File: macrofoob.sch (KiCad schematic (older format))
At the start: 90 parts, among them J2 LED_DATA, J3 POWER, J4 MATRIX_COLUMNS, J5 MATRIX_ROWS, J6 I2C, J7 SSD1306 128x32 OLED, Q1 2N 2222A, SW1 Switch, SW10 Switch, SW11 Switch, SW12 Switch, SW13 Switch, SW14 Switch, SW15 Switch, SW16 Switch, SW17 Switch, SW18 Switch, SW19 Switch, SW2 Switch, SW20 Switch, SW21 Switch, SW22 Switch, SW23 Switch, SW24 Switch, SW25 Switch, SW26 SW_Reset, SW3 Switch, SW4 Switch, SW5 Switch, SW6 Switch, SW7 Switch, SW8 Switch, SW9 Switch

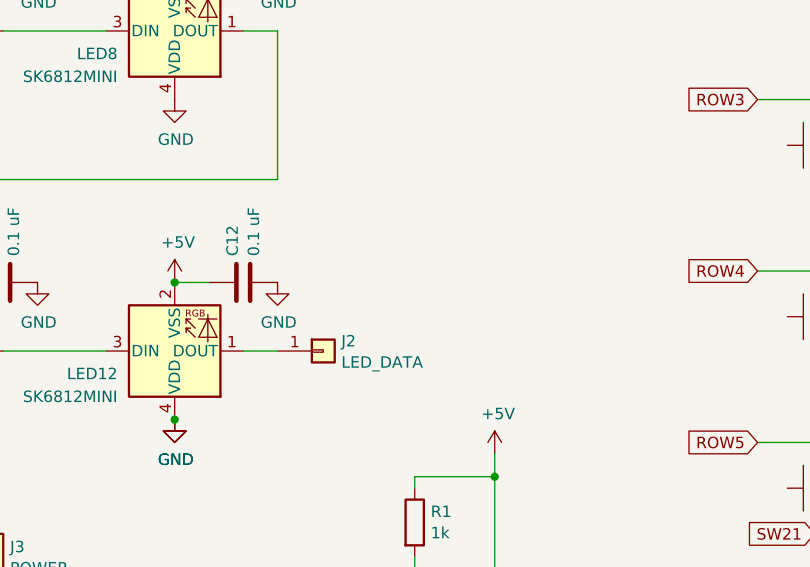
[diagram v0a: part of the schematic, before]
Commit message: updated schematic with more backlight options
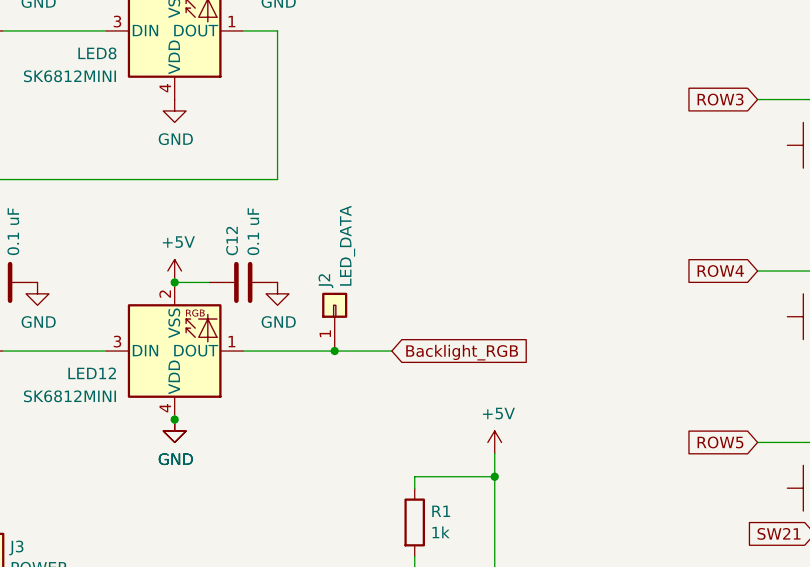
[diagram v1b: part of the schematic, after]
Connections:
- net Backlight_RGB: now reaches J2.1 (Pin_1), LED12.1 (DOUT)
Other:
- moved on the sheet: J2
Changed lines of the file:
@@
 L Connector_Generic:Conn_01x01 J2
 U 1 1 5D751619
-P 5350 4100
-F 0 "J2" H 5429 4143 50  0000 L CNN
-F 1 "LED_DATA" H 5429 4050 50  0000 L CNN
-F 2 "testatur:Generic_Pads_2mm_1x1" H 5350 4100 50  0001 C CNN
-F 3 "~" H 5350 4100 50  0001 C CNN
-	1    5350 4100
-	1    0    0    -1
+P 5400 3900
+F 0 "J2" H 5479 3943 50  0000 L CNN
+F 1 "LED_DATA" H 5479 3850 50  0000 L CNN
+F 2 "testatur:Generic_Pads_2mm_1x1" H 5400 3900 50  0001 C CNN
+F 3 "~" H 5400 3900 50  0001 C CNN
+	1    5400 3900
+	0    -1   -1   0
 $EndComp
-Wire Wire Line
-	5000 4100 5150 4100
 $Comp
 L Connector_Generic:Conn_01x05 J4
@@
 	0    1    1    0
 $EndComp
+Text GLabel 5650 4100 2    50   Input ~ 0
+Backlight_RGB
+Wire Wire Line
+	5000 4100 5400 4100
+Wire Wire Line
+	5400 4100 5650 4100
+Connection ~ 5400 4100
 $EndSCHEMATC

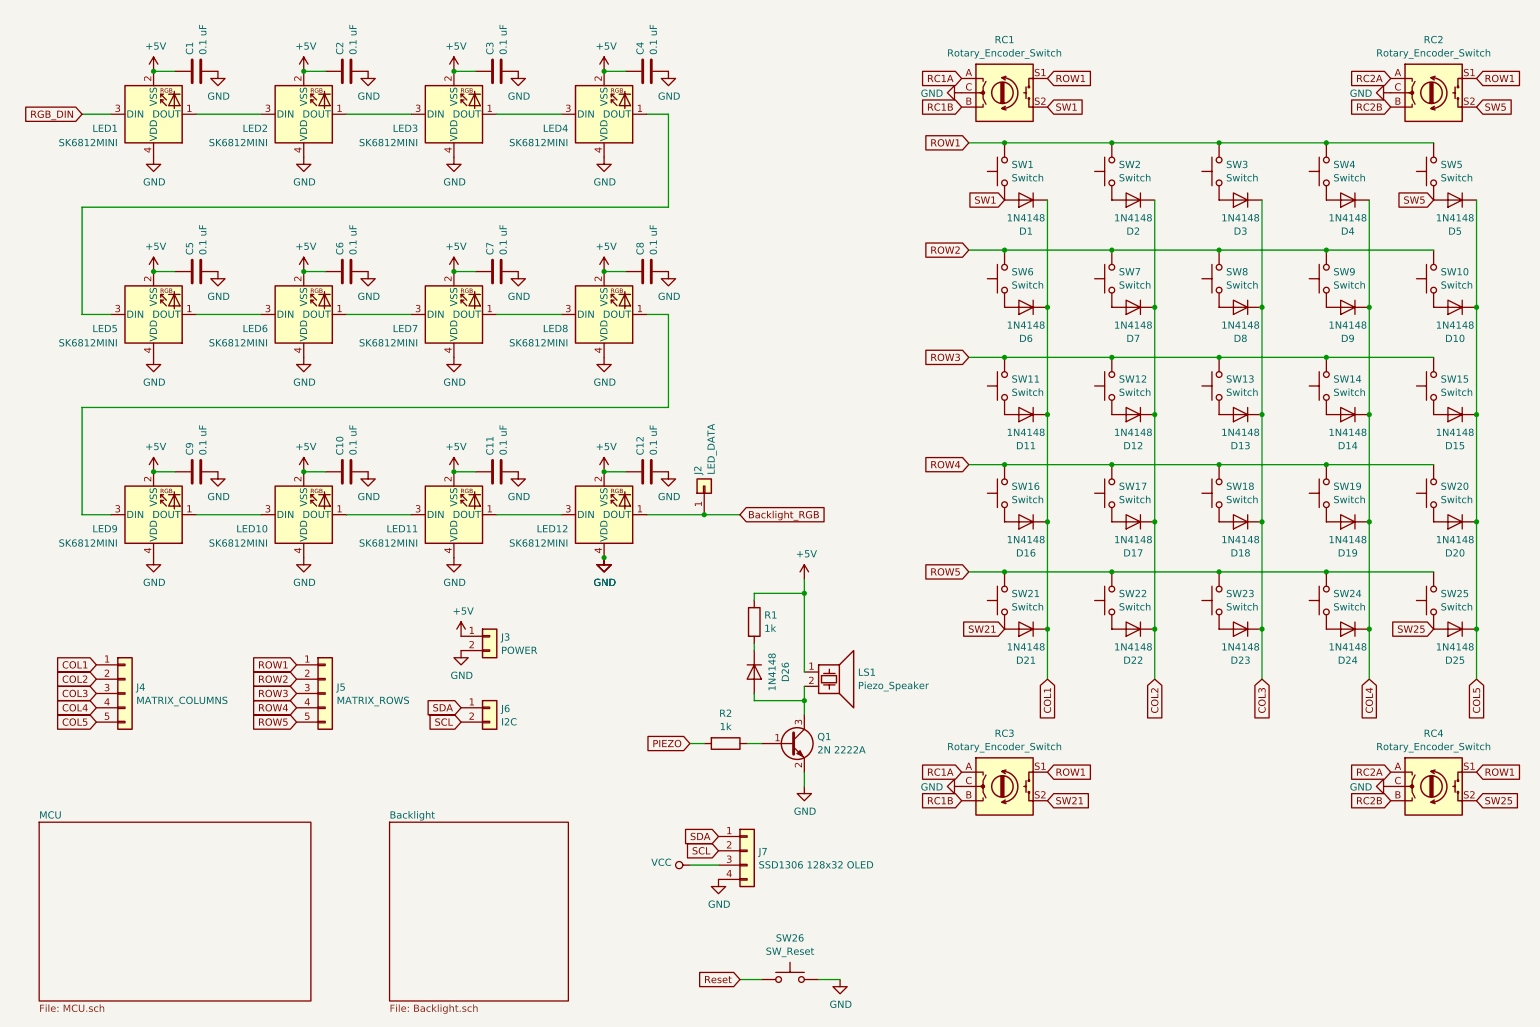
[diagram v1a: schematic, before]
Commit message: new component annotations
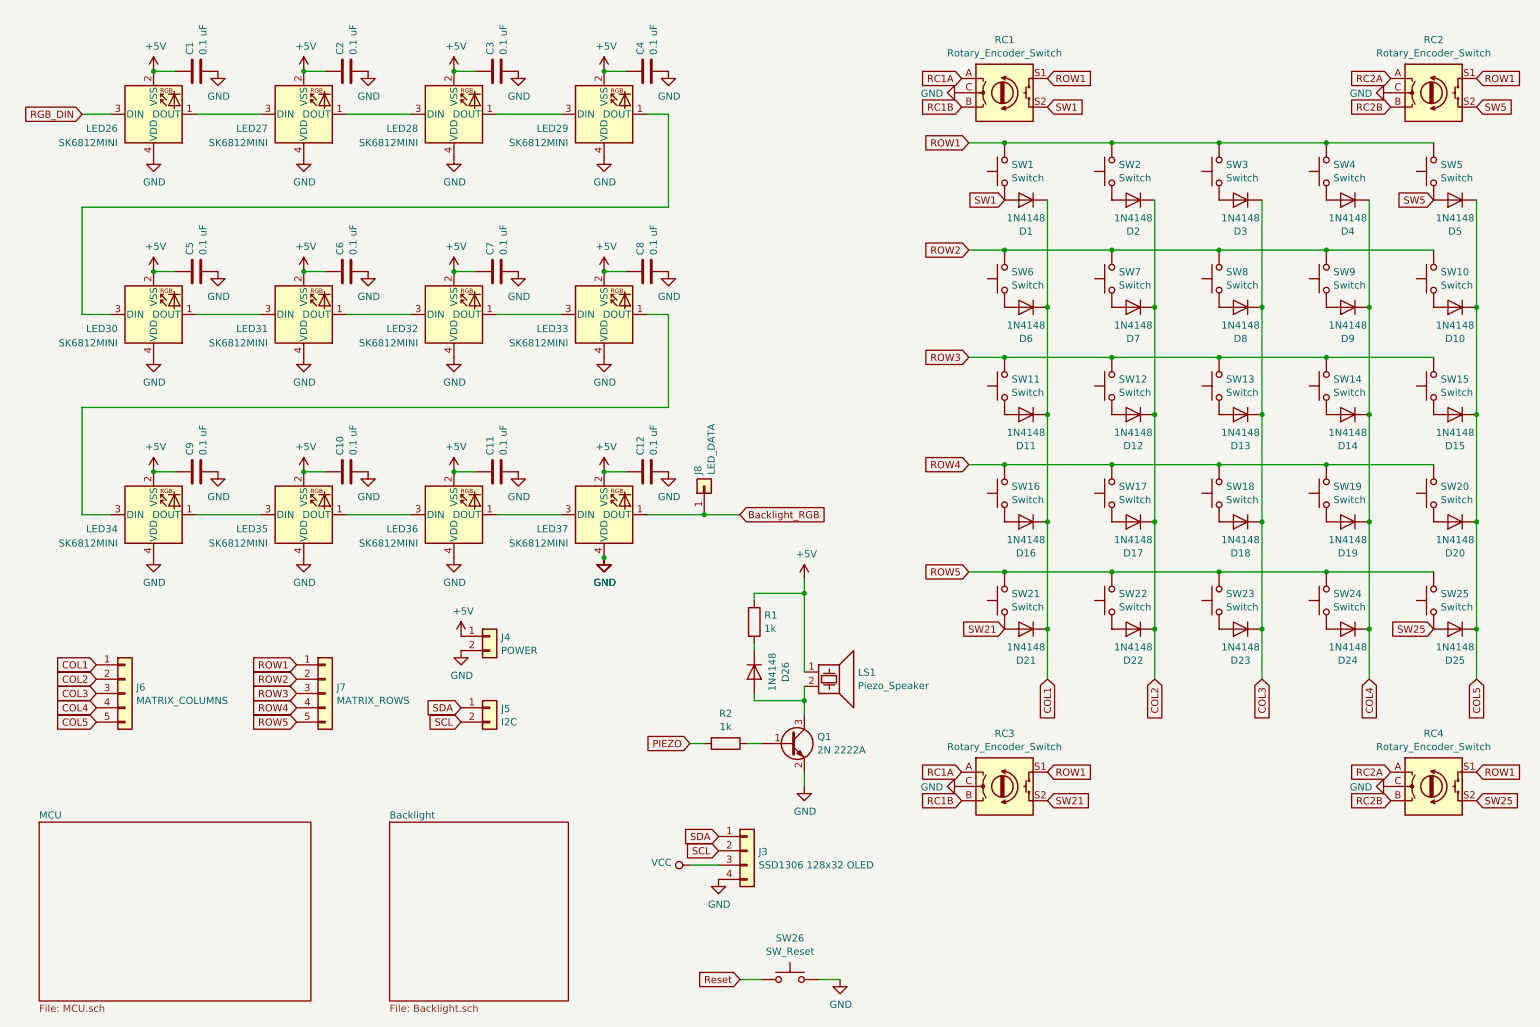
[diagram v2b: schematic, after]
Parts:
- renumbered J7 to J3, J3 to J4, J6 to J5, J4 to J6, J5 to J7, J2 to J8, LED1 to LED26, LED2 to LED27, LED3 to LED28, LED4 to LED29, LED5 to LED30, LED6 to LED31, LED7 to LED32, LED8 to LED33, LED9 to LED34, LED10 to LED35, LED11 to LED36, LED12 to LED37
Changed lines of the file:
@@
 Connection ~ 10800 4150
 $Comp
-L LED:SK6812MINI LED1
+L LED:SK6812MINI LED26
 U 1 1 5D82654C
 P 1550 1300
-F 0 "LED1" H 1300 1400 50  0000 R CNN
+F 0 "LED26" H 1300 1400 50  0000 R CNN
 F 1 "SK6812MINI" H 1300 1500 50  0000 R CNN
 F 2 "LED_SMD:LED_SK6812MINI_PLCC4_3.5x3.5mm_P1.75mm" H 1600 1000 50  0001 L TNN
@@
 $EndComp
 $Comp
-L power:GND #PWR041
+L power:GND #PWR044
 U 1 1 5D9F102E
 P 7200 6000
-F 0 "#PWR041" H 7200 5750 50  0001 C CNN
+F 0 "#PWR044" H 7200 5750 50  0001 C CNN
 F 1 "GND" V 7205 5871 50  0000 R CNN
 F 2 "" H 7200 6000 50  0001 C CNN
@@
 $EndComp
 $Comp
-L power:GND #PWR042
+L power:GND #PWR045
 U 1 1 5D9F103A
 P 10200 6000
-F 0 "#PWR042" H 10200 5750 50  0001 C CNN
+F 0 "#PWR045" H 10200 5750 50  0001 C CNN
 F 1 "GND" V 10205 5871 50  0000 R CNN
 F 2 "" H 10200 6000 50  0001 C CNN
@@
 SW25
 $Comp
-L LED:SK6812MINI LED2
+L LED:SK6812MINI LED27
 U 1 1 5DA35698
 P 2600 1300
-F 0 "LED2" H 2350 1400 50  0000 R CNN
+F 0 "LED27" H 2350 1400 50  0000 R CNN
 F 1 "SK6812MINI" H 2350 1500 50  0000 R CNN
 F 2 "LED_SMD:LED_SK6812MINI_PLCC4_3.5x3.5mm_P1.75mm" H 2650 1000 50  0001 L TNN
@@
 Connection ~ 2600 1000
 $Comp
-L LED:SK6812MINI LED3
+L LED:SK6812MINI LED28
 U 1 1 5DA392F5
 P 3650 1300
-F 0 "LED3" H 3400 1400 50  0000 R CNN
+F 0 "LED28" H 3400 1400 50  0000 R CNN
 F 1 "SK6812MINI" H 3400 1500 50  0000 R CNN
 F 2 "LED_SMD:LED_SK6812MINI_PLCC4_3.5x3.5mm_P1.75mm" H 3700 1000 50  0001 L TNN
@@
 Connection ~ 3650 1000
 $Comp
-L LED:SK6812MINI LED4
+L LED:SK6812MINI LED29
 U 1 1 5DA3CFEE
 P 4700 1300
-F 0 "LED4" H 4450 1400 50  0000 R CNN
+F 0 "LED29" H 4450 1400 50  0000 R CNN
 F 1 "SK6812MINI" H 4450 1500 50  0000 R CNN
 F 2 "LED_SMD:LED_SK6812MINI_PLCC4_3.5x3.5mm_P1.75mm" H 4750 1000 50  0001 L TNN
@@
 	3950 1300 4400 1300
 $Comp
-L LED:SK6812MINI LED5
+L LED:SK6812MINI LED30
 U 1 1 5DA540F9
 P 1550 2700
-F 0 "LED5" H 1300 2800 50  0000 R CNN
+F 0 "LED30" H 1300 2800 50  0000 R CNN
 F 1 "SK6812MINI" H 1300 2900 50  0000 R CNN
 F 2 "LED_SMD:LED_SK6812MINI_PLCC4_3.5x3.5mm_P1.75mm" H 1600 2400 50  0001 L TNN
@@
 Connection ~ 1550 2400
 $Comp
-L LED:SK6812MINI LED6
+L LED:SK6812MINI LED31
 U 1 1 5DA54119
 P 2600 2700
-F 0 "LED6" H 2350 2800 50  0000 R CNN
+F 0 "LED31" H 2350 2800 50  0000 R CNN
 F 1 "SK6812MINI" H 2350 2900 50  0000 R CNN
 F 2 "LED_SMD:LED_SK6812MINI_PLCC4_3.5x3.5mm_P1.75mm" H 2650 2400 50  0001 L TNN
@@
 Connection ~ 2600 2400
 $Comp
-L LED:SK6812MINI LED7
+L LED:SK6812MINI LED32
 U 1 1 5DA54139
 P 3650 2700
-F 0 "LED7" H 3400 2800 50  0000 R CNN
+F 0 "LED32" H 3400 2800 50  0000 R CNN
 F 1 "SK6812MINI" H 3400 2900 50  0000 R CNN
 F 2 "LED_SMD:LED_SK6812MINI_PLCC4_3.5x3.5mm_P1.75mm" H 3700 2400 50  0001 L TNN
@@
 Connection ~ 3650 2400
 $Comp
-L LED:SK6812MINI LED8
+L LED:SK6812MINI LED33
 U 1 1 5DA54159
 P 4700 2700
-F 0 "LED8" H 4450 2800 50  0000 R CNN
+F 0 "LED33" H 4450 2800 50  0000 R CNN
 F 1 "SK6812MINI" H 4450 2900 50  0000 R CNN
 F 2 "LED_SMD:LED_SK6812MINI_PLCC4_3.5x3.5mm_P1.75mm" H 4750 2400 50  0001 L TNN
@@
 	3950 2700 4400 2700
 $Comp
-L LED:SK6812MINI LED9
+L LED:SK6812MINI LED34
 U 1 1 5DA5C5A4
 P 1550 4100
-F 0 "LED9" H 1300 4200 50  0000 R CNN
+F 0 "LED34" H 1300 4200 50  0000 R CNN
 F 1 "SK6812MINI" H 1300 4300 50  0000 R CNN
 F 2 "LED_SMD:LED_SK6812MINI_PLCC4_3.5x3.5mm_P1.75mm" H 1600 3800 50  0001 L TNN
@@
 Connection ~ 1550 3800
 $Comp
-L LED:SK6812MINI LED10
+L LED:SK6812MINI LED35
 U 1 1 5DA5C5C4
 P 2600 4100
-F 0 "LED10" H 2350 4200 50  0000 R CNN
+F 0 "LED35" H 2350 4200 50  0000 R CNN
 F 1 "SK6812MINI" H 2350 4300 50  0000 R CNN
 F 2 "LED_SMD:LED_SK6812MINI_PLCC4_3.5x3.5mm_P1.75mm" H 2650 3800 50  0001 L TNN
@@
 Connection ~ 2600 3800
 $Comp
-L LED:SK6812MINI LED11
+L LED:SK6812MINI LED36
 U 1 1 5DA5C5E4
 P 3650 4100
-F 0 "LED11" H 3400 4200 50  0000 R CNN
+F 0 "LED36" H 3400 4200 50  0000 R CNN
 F 1 "SK6812MINI" H 3400 4300 50  0000 R CNN
 F 2 "LED_SMD:LED_SK6812MINI_PLCC4_3.5x3.5mm_P1.75mm" H 3700 3800 50  0001 L TNN
@@
 Connection ~ 3650 3800
 $Comp
-L LED:SK6812MINI LED12
+L LED:SK6812MINI LED37
 U 1 1 5DA5C604
 P 4700 4100
-F 0 "LED12" H 4450 4200 50  0000 R CNN
+F 0 "LED37" H 4450 4200 50  0000 R CNN
 F 1 "SK6812MINI" H 4450 4300 50  0000 R CNN
 F 2 "LED_SMD:LED_SK6812MINI_PLCC4_3.5x3.5mm_P1.75mm" H 4750 3800 50  0001 L TNN
@@
 $EndComp
 $Comp
-L power:GND #PWR038
+L power:GND #PWR039
 U 1 1 5DA5C616
 P 4700 4400
-F 0 "#PWR038" H 4700 4150 50  0001 C CNN
+F 0 "#PWR039" H 4700 4150 50  0001 C CNN
 F 1 "GND" H 4705 4225 50  0000 C CNN
 F 2 "" H 4700 4400 50  0001 C CNN
@@
 	6100 4650 5750 4650
 $Comp
-L power:+5V #PWR044
+L power:+5V #PWR040
 U 1 1 5D6D3E04
 P 6100 4550
-F 0 "#PWR044" H 6100 4400 50  0001 C CNN
+F 0 "#PWR040" H 6100 4400 50  0001 C CNN
 F 1 "+5V" H 6115 4725 50  0000 C CNN
 F 2 "" H 6100 4550 50  0001 C CNN
@@
 	5750 5000 5750 5050
 $Comp
-L Connector_Generic:Conn_01x04 J7
+L Connector_Generic:Conn_01x04 J3
 U 1 1 5D6C8E16
 P 5700 6450
-F 0 "J7" H 5780 6443 50  0000 L CNN
+F 0 "J3" H 5780 6443 50  0000 L CNN
 F 1 "SSD1306 128x32 OLED" H 5780 6350 50  0000 L CNN
 F 2 "Connector_PinHeader_2.54mm:PinHeader_1x04_P2.54mm_Vertical" H 5700 6450 50  0001 C CNN
@@
 $EndComp
 $Comp
-L power:GND #PWR0101
+L power:GND #PWR047
 U 1 1 5D6CADAB
 P 5500 6650
-F 0 "#PWR0101" H 5500 6400 50  0001 C CNN
+F 0 "#PWR047" H 5500 6400 50  0001 C CNN
 F 1 "GND" H 5505 6475 50  0000 C CNN
 F 2 "" H 5500 6650 50  0001 C CNN
@@
 SDA
 $Comp
-L power:VCC #PWR0103
+L power:VCC #PWR046
 U 1 1 5D6CE66C
 P 5300 6550
-F 0 "#PWR0103" H 5300 6400 50  0001 C CNN
+F 0 "#PWR046" H 5300 6400 50  0001 C CNN
 F 1 "VCC" V 5318 6678 50  0000 L CNN
 F 2 "" H 5300 6550 50  0001 C CNN
@@
 Reset
 $Comp
-L power:GND #PWR039
+L power:GND #PWR038
 U 1 1 5D81904B
 P 4700 4400
-F 0 "#PWR039" H 4700 4150 50  0001 C CNN
+F 0 "#PWR038" H 4700 4150 50  0001 C CNN
 F 1 "GND" H 4705 4225 50  0000 C CNN
 F 2 "" H 4700 4400 50  0001 C CNN
@@
 Connection ~ 4700 4400
 $Comp
-L power:GND #PWR046
+L power:GND #PWR048
 U 1 1 5D819078
 P 6350 7350
-F 0 "#PWR046" H 6350 7100 50  0001 C CNN
+F 0 "#PWR048" H 6350 7100 50  0001 C CNN
 F 1 "GND" H 6355 7175 50  0000 C CNN
 F 2 "" H 6350 7350 50  0001 C CNN
@@
 	6200 7350 6350 7350
 $Comp
-L Connector_Generic:Conn_01x02 J3
+L Connector_Generic:Conn_01x02 J4
 U 1 1 5D74E4BE
 P 3900 4950
-F 0 "J3" H 3980 4943 50  0000 L CNN
+F 0 "J4" H 3980 4943 50  0000 L CNN
 F 1 "POWER" H 3980 4850 50  0000 L CNN
 F 2 "testatur:Generic_Pads_2mm_1x2" H 3900 4950 50  0001 C CNN
@@
 $EndComp
 $Comp
-L Connector_Generic:Conn_01x02 J6
+L Connector_Generic:Conn_01x02 J5
 U 1 1 5D74F5A4
 P 3900 5450
-F 0 "J6" H 3980 5443 50  0000 L CNN
+F 0 "J5" H 3980 5443 50  0000 L CNN
 F 1 "I2C" H 3980 5350 50  0000 L CNN
 F 2 "testatur:Generic_Pads_2mm_1x2" H 3900 5450 50  0001 C CNN
@@
 $EndComp
 $Comp
-L Connector_Generic:Conn_01x05 J5
+L Connector_Generic:Conn_01x05 J7
 U 1 1 5D7503CC
 P 2750 5350
-F 0 "J5" H 2830 5393 50  0000 L CNN
+F 0 "J7" H 2830 5393 50  0000 L CNN
 F 1 "MATRIX_ROWS" H 2830 5300 50  0000 L CNN
 F 2 "testatur:Generic_Pads_2mm_1x5" H 2750 5350 50  0001 C CNN
@@
 $EndComp
 $Comp
-L Connector_Generic:Conn_01x01 J2
+L Connector_Generic:Conn_01x01 J8
 U 1 1 5D751619
 P 5400 3900
-F 0 "J2" H 5479 3943 50  0000 L CNN
+F 0 "J8" H 5479 3943 50  0000 L CNN
 F 1 "LED_DATA" H 5479 3850 50  0000 L CNN
 F 2 "testatur:Generic_Pads_2mm_1x1" H 5400 3900 50  0001 C CNN
@@
 $EndComp
 $Comp
-L Connector_Generic:Conn_01x05 J4
+L Connector_Generic:Conn_01x05 J6
 U 1 1 5D75615C
 P 1350 5350
-F 0 "J4" H 1429 5393 50  0000 L CNN
+F 0 "J6" H 1429 5393 50  0000 L CNN
 F 1 "MATRIX_COLUMNS" H 1429 5300 50  0000 L CNN
 F 2 "testatur:Generic_Pads_2mm_1x5" H 1350 5350 50  0001 C CNN
@@
 SCL
 $Comp
-L power:GND #PWR045
+L power:GND #PWR042
 U 1 1 5D758616
 P 3700 5050
-F 0 "#PWR045" H 3700 4800 50  0001 C CNN
+F 0 "#PWR042" H 3700 4800 50  0001 C CNN
 F 1 "GND" H 3705 4875 50  0000 C CNN
 F 2 "" H 3700 5050 50  0001 C CNN
@@
 $EndComp
 $Comp
-L power:+5V #PWR040
+L power:+5V #PWR041
 U 1 1 5D758B00
 P 3700 4950
-F 0 "#PWR040" H 3700 4800 50  0001 C CNN
+F 0 "#PWR041" H 3700 4800 50  0001 C CNN
 F 1 "+5V" H 3715 5125 50  0000 C CNN
 F 2 "" H 3700 4950 50  0001 C CNN

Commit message: fixed power flags
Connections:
- net +5V is gone; now on net VCC: C1.1, C10.1, C11.1, C12.1, C2.1, C3.1, C4.1, C5.1, C6.1, C7.1, C8.1, C9.1, J4.1 (Pin_1), LED26.2 (VSS), LED27.2 (VSS), LED28.2 (VSS), LED29.2 (VSS), LED30.2 (VSS), LED31.2 (VSS), LED32.2 (VSS), LED33.2 (VSS), LED34.2 (VSS), LED35.2 (VSS), LED36.2 (VSS), LED37.2 (VSS), LS1.1, R1.1
